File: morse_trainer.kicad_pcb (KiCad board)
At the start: 2 copper layers, 18 parts, among them J1 AVR-ISP-6, SW1 SW_Push, U1 ATtiny2313-20SU, U2 RC1602A

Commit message: Schematics done !
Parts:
- added J2: Conn_01x02, Connector_PinHeader_2.54mm:PinHeader_1x02_P2.54mm_Vertical, F.Cu at (48.9, 27.3)
- moved RV1 44.5 mm to (54.8, 65.2), turned to 270 degrees
- moved R6 36.7 mm to (48.7, 31.8), turned to 270 degrees
- moved H1 32.0 mm to (63.0, 65.0)
- moved J1 29.6 mm to (54.5, 34.5), turned to 180 degrees
- moved C1 29.4 mm to (54.6, 58.7), turned to 180 degrees
- moved R4 28.5 mm to (59.2, 58.6)
- moved RV2 27.7 mm to (49.7, 39.6), turned to 90 degrees
- moved R5 26.9 mm to (49.8, 61.8)
- moved R1 26.3 mm to (54.6, 61.3)
- moved U1 21.1 mm to (54.6, 49.7), turned to 180 degrees
- moved SW1 20.0 mm to (63.4, 52.7)
- moved C3 16.0 mm to (57.1, 29.1), turned to 90 degrees
- moved R3 15.7 mm to (62.0, 39.1), turned to 180 degrees
- moved BZ1 12.1 mm to (62.0, 33.0), turned to 90 degrees
- moved R2 10.1 mm to (62.0, 41.5)
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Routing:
- net GND: track 0.00 -> 103.1 mm
- net VCC: track 0.00 -> 66.2 mm
- net /DB7: track 0.00 -> 45.1 mm
- net /~RST: track 0.00 -> 38.4 mm
- net /DB6: track 0.00 -> 28.2 mm
- net /SCK: track 0.00 -> 24.7 mm
- net Net-(R6-Pad2): track 0.00 -> 14.8 mm
- net /RS: track 0.00 -> 13.7 mm
- net /R\~W: track 0.00 -> 12.4 mm
- net /E: track 0.00 -> 11.1 mm
- net Net-(BZ1-Pad1): track 0.00 -> 9.22 mm
- net /DB5: track 0.00 -> 8.90 mm
- net Net-(RV1-Pad2): track 0.00 -> 8.37 mm
- net /DB4: track 0.00 -> 7.63 mm
- net Net-(SW1-Pad1): track 0.00 -> 7.40 mm
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- added copper zone on B.Cu, net GND
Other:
- board outline added: 24.4 x 43.2 mm

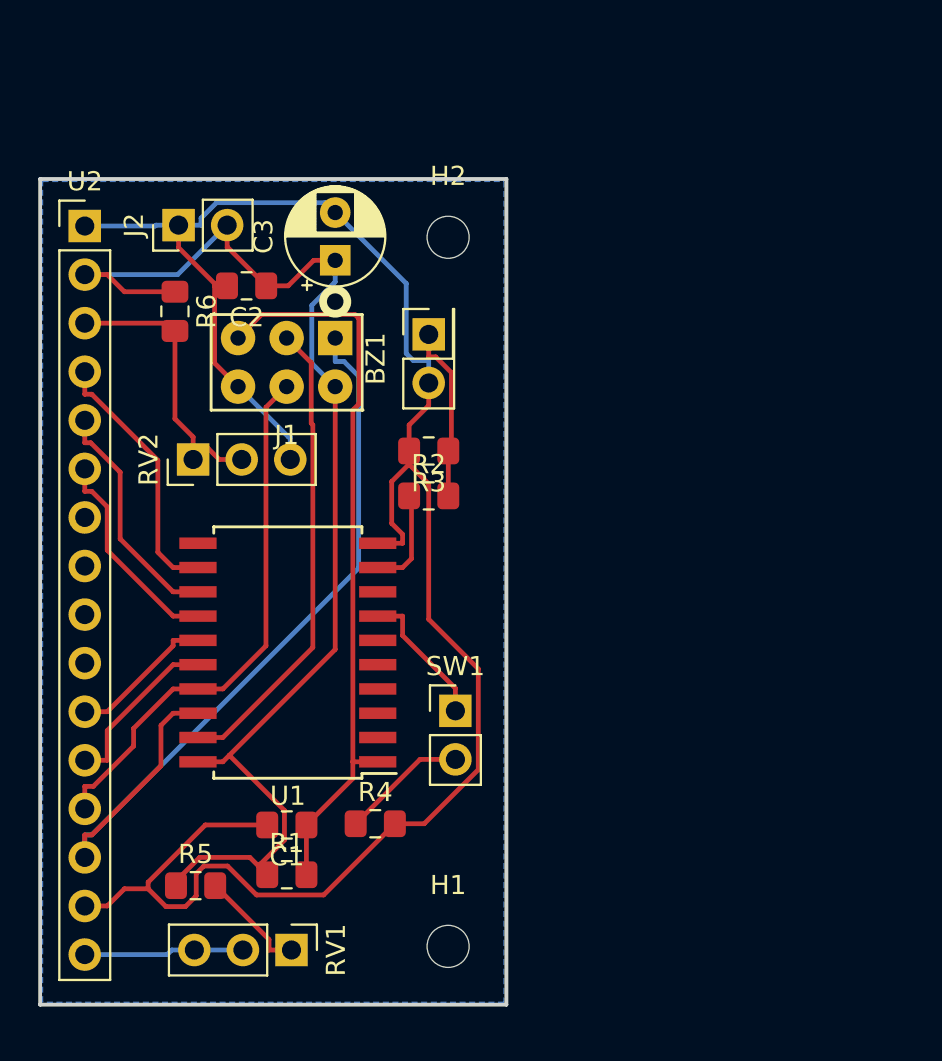
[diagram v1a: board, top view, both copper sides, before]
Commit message: add 2 10 pin connector to the schematic \n first version of the boad is done
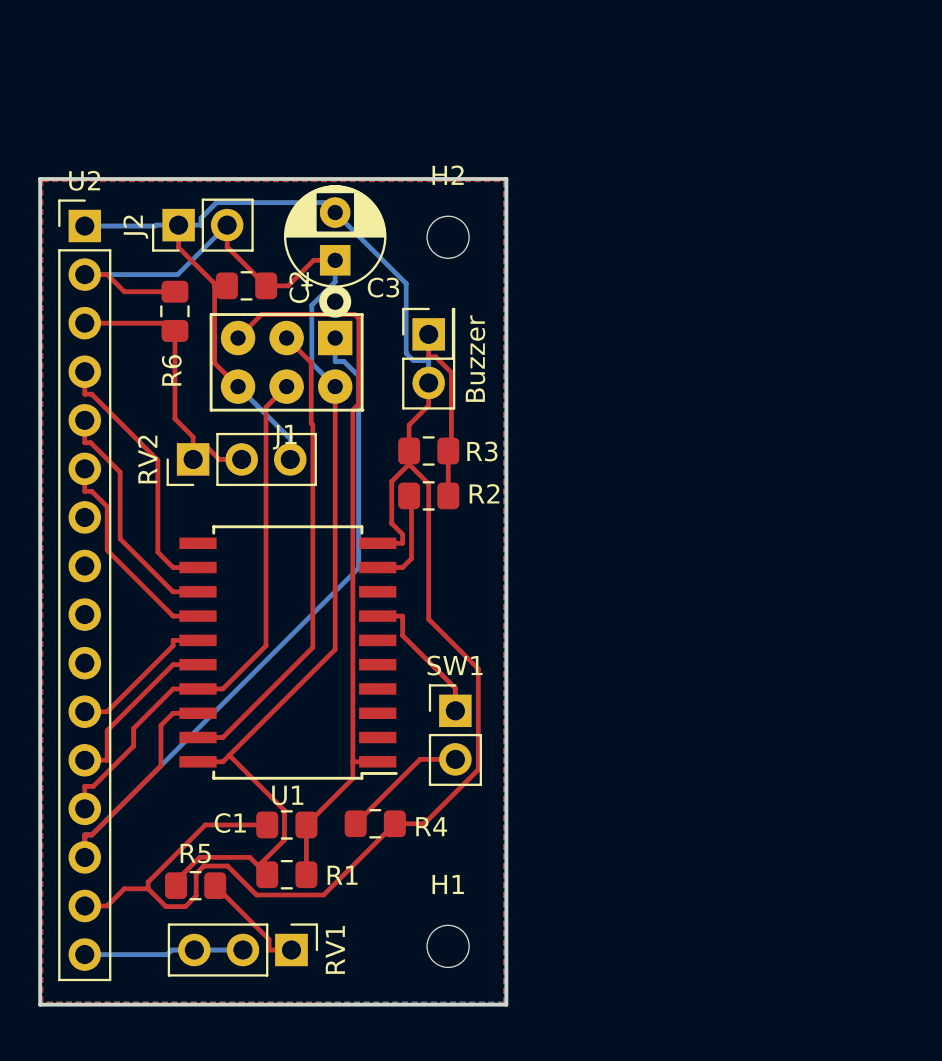
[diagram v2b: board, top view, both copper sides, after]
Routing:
- added copper zone on F.Cu, net GND
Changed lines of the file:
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@@
     (tags "capacitor handsolder")
     (attr smd)
-    (fp_text reference C1 (at 0 -1.65 180) (layer F.SilkS)
+    (fp_text reference C1 (at 2.93 0.0635 180) (layer F.SilkS)
       (effects (font (size 1 1) (thickness 0.15)))
     )
@@
     (tags "capacitor handsolder")
     (attr smd)
-    (fp_text reference C2 (at 0 -1.65 180) (layer F.SilkS)
+    (fp_text reference C2 (at -2.794 -0.0635 270) (layer F.SilkS)
       (effects (font (size 1 1) (thickness 0.15)))
     )
@@
     (descr "CP, Radial series, Radial, pin pitch=2.50mm, , diameter=5mm, Electrolytic Capacitor")
     (tags "CP Radial series Radial pin pitch 2.50mm  diameter 5mm Electrolytic Capacitor")
-    (fp_text reference C3 (at 1.25 -3.75 90) (layer F.SilkS)
+    (fp_text reference C3 (at -1.4605 2.54 180) (layer F.SilkS)
       (effects (font (size 1 1) (thickness 0.15)))
     )
@@
     (tags "resistor handsolder")
     (attr smd)
-    (fp_text reference R1 (at 0 -1.65) (layer F.SilkS)
+    (fp_text reference R1 (at 2.912 0.0635) (layer F.SilkS)
       (effects (font (size 1 1) (thickness 0.15)))
     )
@@
     (tags "resistor handsolder")
     (attr smd)
-    (fp_text reference R2 (at 0 -1.65) (layer F.SilkS)
+    (fp_text reference R2 (at 2.921 -0.0635) (layer F.SilkS)
       (effects (font (size 1 1) (thickness 0.15)))
     )
@@
     (tags "resistor handsolder")
     (attr smd)
-    (fp_text reference R3 (at 0 -1.65 180) (layer F.SilkS)
+    (fp_text reference R3 (at -2.794 -0.0635 180) (layer F.SilkS)
       (effects (font (size 1 1) (thickness 0.15)))
     )
@@
     (tags "resistor handsolder")
     (attr smd)
-    (fp_text reference R4 (at 0 -1.65) (layer F.SilkS)
+    (fp_text reference R4 (at 2.921 0.1905) (layer F.SilkS)
       (effects (font (size 1 1) (thickness 0.15)))
     )
@@
     (tags "resistor handsolder")
     (attr smd)
-    (fp_text reference R6 (at 0 -1.65 270) (layer F.SilkS)
+    (fp_text reference R6 (at 3.1115 0.127 270) (layer F.SilkS)
       (effects (font (size 1 1) (thickness 0.15)))
     )
@@
       (effects (font (size 1 1) (thickness 0.15)))
     )
-    (fp_text value 1k (at 0 7.41 90) (layer F.Fab)
+    (fp_text value 1k (at -0.1905 7.5565 90) (layer F.Fab)
       (effects (font (size 1 1) (thickness 0.15)))
     )
@@
       (effects (font (size 1 1) (thickness 0.15)))
     )
-    (fp_text value SW_Push (at 0 4.87) (layer F.Fab)
+    (fp_text value SW_Push (at 1.9685 1.016 90) (layer F.Fab)
       (effects (font (size 1 1) (thickness 0.15)))
     )
@@
     (descr "Through hole straight socket strip, 2x01, 2.54mm pitch, double cols (from Kicad 4.0.7), script generated")
     (tags "Through hole socket strip THT 2x01 2.54mm double row")
-    (fp_text reference BZ1 (at -1.27 -2.77 90) (layer F.SilkS)
-      (effects (font (size 1 1) (thickness 0.15)))
-    )
-    (fp_text value Buzzer (at -1.27 2.77 90) (layer F.Fab)
+    (fp_text reference BZ1 (at -1.27 -2.413 90) (layer F.Fab)
+      (effects (font (size 1 1) (thickness 0.15)))
+    )
+    (fp_text value Buzzer (at -1.3335 2.4765 90) (layer F.SilkS)
       (effects (font (size 1 1) (thickness 0.15)))
     )
@@
       )
     )
+  )
+  (zone (net 2) (net_name GND) (layer F.Cu) (hatch edge 0.508)
+    (connect_pads (clearance 0.508))
+    (min_thickness 0.254)
+    (fill yes (arc_segments 16) (thermal_gap 0.508) (thermal_bridge_width 0.508))
+    (polygon
+      (pts
+        (xy 65.913 68.0085) (xy 41.783 67.945) (xy 41.783 25.019) (xy 65.913 25.019)
+      )
+    )
